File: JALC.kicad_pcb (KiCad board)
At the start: 2 copper layers, 30 x 55 mm, 5 parts, among them J1 Conn_01x03, U1 WeMos_D1_mini

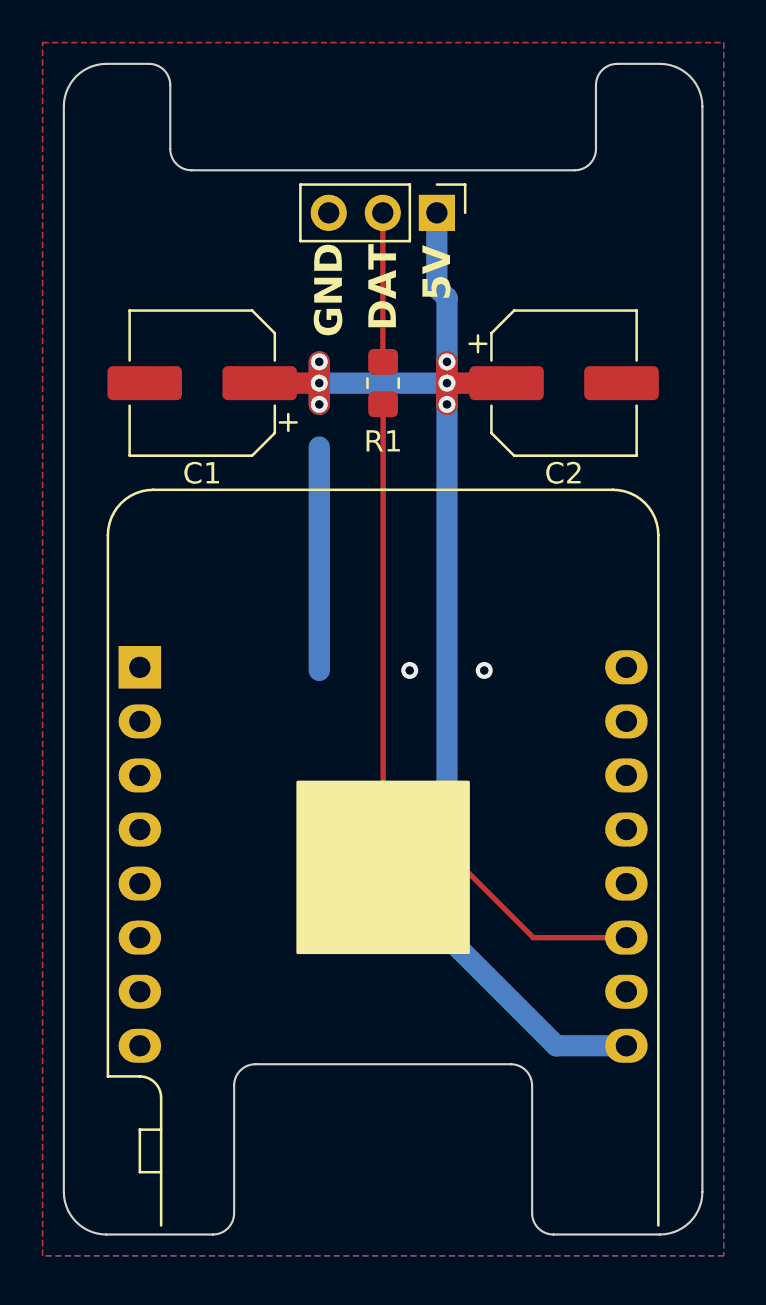
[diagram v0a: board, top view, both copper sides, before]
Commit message: Added REV2.0 (ESP32-C3)
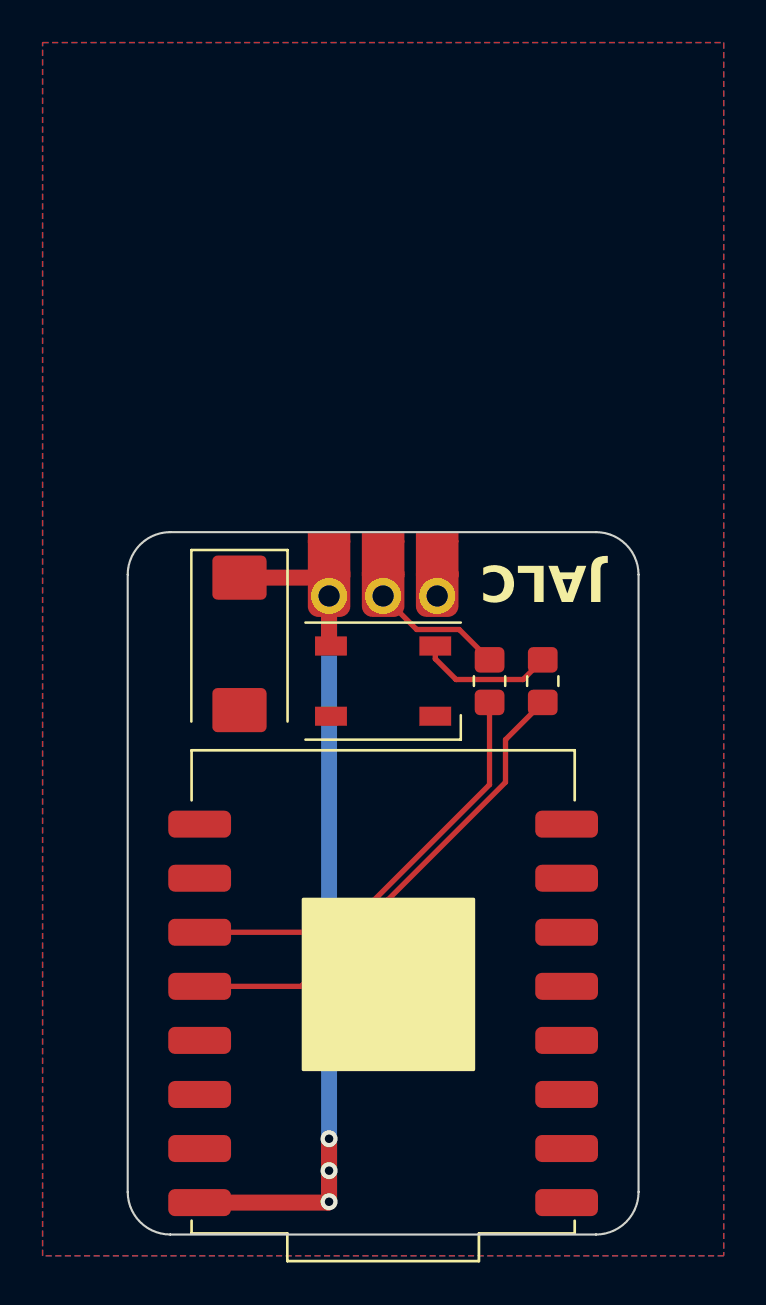
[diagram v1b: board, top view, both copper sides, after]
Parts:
- removed C2: 470UF, Capacitor_SMD:CP_Elec_6.3x7.7
- added D1: WS2812B, LED_SMD:LED_WS2812B_PLCC4_5.0x5.0mm_P3.2mm, F.Cu at (145.0, 89.0)
- added R2: 470R, Resistor_SMD:R_0805_2012Metric_Pad1.20x1.40mm_HandSolder, F.Cu at (150.0, 89.0)
- C1: value 470UF -> 1000uF; footprint Capacitor_SMD:CP_Elec_6.3x7.7 -> Capacitor_Tantalum_SMD:CP_EIA-7343-43_Kemet-X
- J1: footprint Connector_PinHeader_2.54mm:PinHeader_1x03_P2.54mm_Vertical -> SolderConnector:SolderConnector
- U1: value WeMos_D1_mini -> ESP32-C3_SUPERMINI; footprint Module:WEMOS_D1_mini_light -> MODULE_ESP32-C3_SUPERMINI:MODULE_ESP32-C3_SUPERMINI
- moved U1 19.1 mm to (145.0, 103.6), turned to 180 degrees
- moved J1 17.2 mm to (145.0, 84.0), turned to 0 degrees
- moved R1 15.9 mm to (152.5, 89.0)
- moved C1 12.4 mm to (138.2, 87.2), turned to -90 degrees
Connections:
- R1 pad 1: Net-(U1-D4) -> GPIO3
- R1 pad 2: Net-(J1-Pin_2) -> Net-(D1-DIN)
- U1 pad 10: GND -> unconnected-(U1-GPIO10-Pad10)
- U1 pad 2: unconnected-(U1-A0-Pad2) -> GPIO2
- U1 pad 3: unconnected-(U1-D0-Pad3) -> GPIO3
- U1 pad 9: +5V -> unconnected-(U1-GPIO9-Pad9)
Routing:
- net Net-(U1-D4): track 32.4 -> 0.00 mm
- net GPIO3: track 0.00 -> 22.8 mm
- net GPIO2: track 0.00 -> 20.4 mm
- net +5V: track 63.4 -> 44.2 mm, vias 6 -> 3
- net GND: track 10.5 -> 0.00 mm, vias 2 -> 0
- net Net-(D1-DIN): track 0.00 -> 6.44 mm
- net Net-(J1-Pin_2): track 7.01 -> 6.24 mm
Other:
- board size 30 x 55 mm -> 24 x 33 mm
- board text added: "REV2.0 2024/10 github.com/foorschtbar/JALC"
- board text removed: "REV1.0 2024/09 github.com/foorschtbar/JALC"
